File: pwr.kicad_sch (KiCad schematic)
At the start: 11 parts, among them U5 TPS561208DDCR

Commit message: Updated Schematic
Updated parts of todo list for schematic
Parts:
- added C5: .1uF, symbol Device:C_Small
- C1: value 44muF -> 22uF
- C2: value 20.1muF -> 22uF
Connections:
- net 12 V: now also C5.1
- net GND: now also C5.2
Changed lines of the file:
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@@
+	)
+	(junction
+		(at 62.23 41.91)
+		(diameter 0)
+		(color 0 0 0 0)
 	)
 	(junction
@@
 	(wire
 		(pts
-			(xy 49.53 41.91) (xy 66.04 41.91)
+			(xy 49.53 41.91) (xy 62.23 41.91)
 		)
 		(stroke
@@
 		(pts
 			(xy 157.48 26.67) (xy 157.48 46.99)
+		)
+		(stroke
+			(width 0)
+			(type default)
+		)
+	)
+	(wire
+		(pts
+			(xy 62.23 41.91) (xy 66.04 41.91)
 		)
 		(stroke
@@
 			)
 		)
-		(property "Value" "20.1muF"
+		(property "Value" "22uF"
 			(at 72.39 45.7262 0)
 			(show_name no)
@@
 			)
 		)
-		(property "Value" "44muF"
+		(property "Value" "22uF"
 			(at 137.16 40.6462 0)
 			(show_name no)
@@
 	)
 	(symbol
+		(lib_id "Device:C_Small")
+		(at 62.23 44.45 0)
+		(unit 1)
+		(body_style 1)
+		(exclude_from_sim no)
+		(in_bom yes)
+		(on_board yes)
+		(in_pos_files yes)
+		(dnp no)
+		(fields_autoplaced yes)
+		(property "Reference" "C5"
+			(at 64.77 43.1862 0)
+			(show_name no)
+			(do_not_autoplace no)
+			(effects
+				(font
+					(size 1.27 1.27)
+				)
+				(justify left)
+			)
+		)
+		(property "Value" ".1uF"
+			(at 64.77 45.7262 0)
+			(show_name no)
+			(do_not_autoplace no)
+			(effects
+				(font
+					(size 1.27 1.27)
+				)
+				(justify left)
+			)
+		)
+		(property "Footprint" ""
+			(at 62.23 44.45 0)
+			(hide yes)
+			(show_name no)
+			(do_not_autoplace no)
+			(effects
+				(font
+					(size 1.27 1.27)
+				)
+			)
+		)
+		(property "Datasheet" ""
+			(at 62.23 44.45 0)
+			(hide yes)
+			(show_name no)
+			(do_not_autoplace no)
+			(effects
+				(font
+					(size 1.27 1.27)
+				)
+			)
+		)
+		(property "Description" "Unpolarized capacitor, small symbol"
+			(at 62.23 44.45 0)
+			(hide yes)
+			(show_name no)
+			(do_not_autoplace no)
+			(effects
+				(font
+					(size 1.27 1.27)
+				)
+			)
+		)
+		(pin "2"
+		)
+		(pin "1"
+		)
+		(instances
+			(project "X19-Float-Board"
+				(path "/00000000-0000-0000-0000-000060e6118b/dfdc99bd-6797-4c58-8fa3-5fd2e2701b4c"
+					(reference "C5")
+					(unit 1)
+				)
+			)
+		)
+	)
+	(symbol
 		(lib_id "Device:R_Small_US")
 		(at 81.28 31.75 0)
@@
 					(unit 1)
 				)
+			)
+		)
+	)
+	(symbol
+		(lib_id "power:GND")
+		(at 62.23 46.99 0)
+		(unit 1)
+		(body_style 1)
+		(exclude_from_sim no)
+		(in_bom yes)
+		(on_board yes)
+		(in_pos_files yes)
+		(dnp no)
+		(fields_autoplaced yes)
+		(property "Reference" "#PWR029"
+			(at 62.23 53.34 0)
+			(hide yes)
+			(show_name no)
+			(do_not_autoplace no)
+			(effects
+				(font
+					(size 1.27 1.27)
+				)
+			)
+		)
+		(property "Value" "GND"
+			(at 62.23 52.07 0)
+			(show_name no)
+			(do_not_autoplace no)
+			(effects
+				(font
+					(size 1.27 1.27)
+				)
+			)
+		)
+		(property "Footprint" ""
+			(at 62.23 46.99 0)
+			(hide yes)
+			(show_name no)
+			(do_not_autoplace no)
+			(effects
+				(font
+					(size 1.27 1.27)
+				)
+			)
+		)
+		(property "Datasheet" ""
+			(at 62.23 46.99 0)
+			(hide yes)
+			(show_name no)
+			(do_not_autoplace no)
+			(effects
+				(font
+					(size 1.27 1.27)
+				)
+			)
+		)
+		(property "Description" "Power symbol creates a global label with name \"GND\" , ground"
+			(at 62.23 46.99 0)
+			(hide yes)
+			(show_name no)
+			(do_not_autoplace no)
+			(effects
+				(font
+					(size 1.27 1.27)
+				)
+			)
+		)
+		(pin "1"
+		)
+		(instances
+			(project "X19-Float-Board"
+				(path "/00000000-0000-0000-0000-000060e6118b/dfdc99bd-6797-4c58-8fa3-5fd2e2701b4c"
+					(reference "#PWR029")
+					(unit 1)
+				)

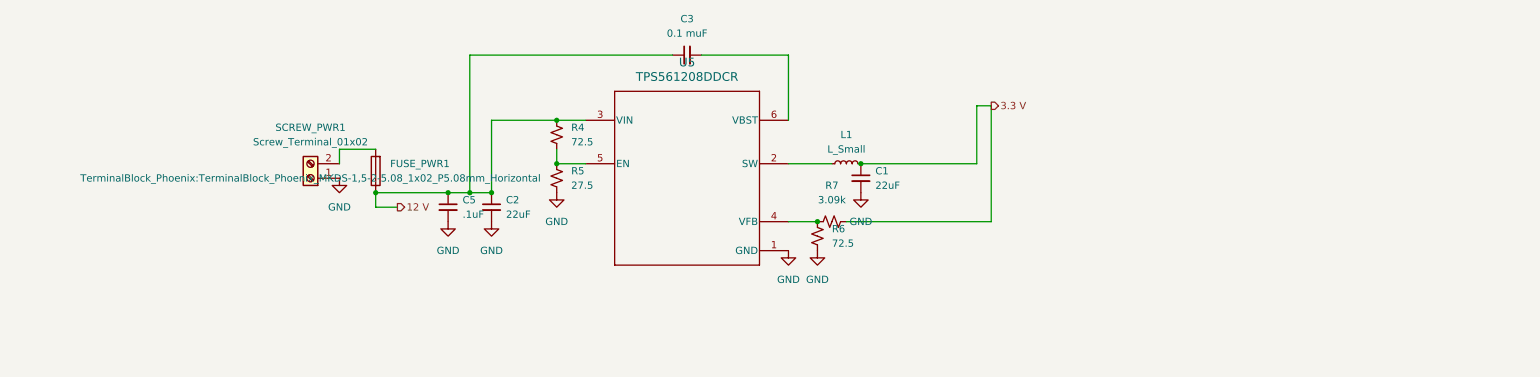
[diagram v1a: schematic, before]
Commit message: Updated Schematic
Updated schematic
Cleaned up dense portions
added H bridge
correct i2c wiring
added ferrite beads
added 12 V power monitoring
added stlink
added power mux
added power from usb
reformatted hierarichal sheets
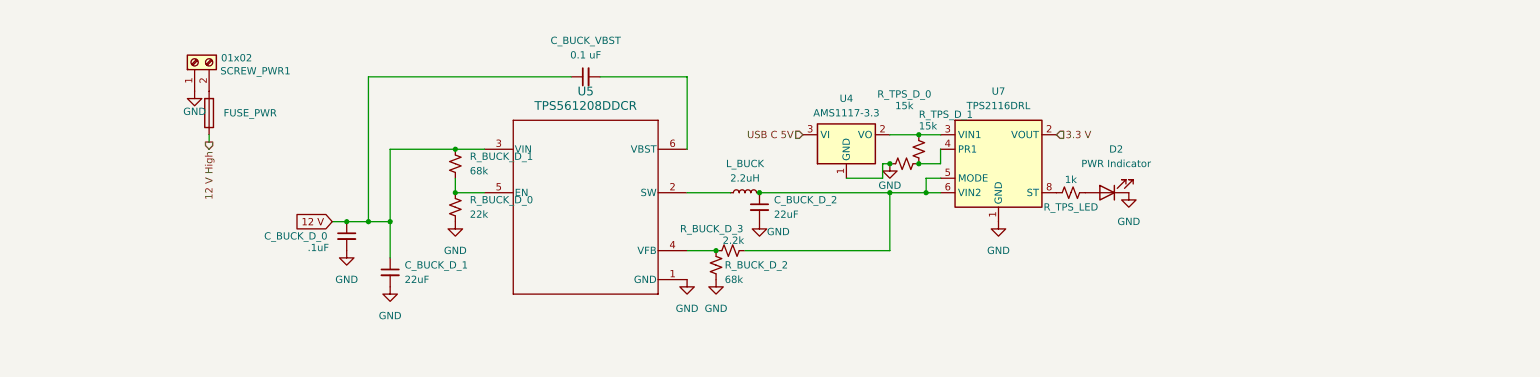
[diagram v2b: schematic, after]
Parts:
- added D2: PWR Indicator, symbol Device:LED
- added R_TPS_D_0, R_TPS_D_1: 15k, symbol Device:R_Small_US
- added R_TPS_LED: 1k, symbol Device:R_Small_US
- added U4: AMS1117-3.3, Package_TO_SOT_SMD:SOT-223-3_TabPin2, symbol Regulator_Linear:AMS1117-3.3
- added U7: TPS2116DRL, Package_TO_SOT_SMD:SOT-583-8, symbol Power_Management:TPS2116DRL
- C_BUCK_VBST: renamed from C3; value 0.1 muF -> 0.1 uF
- L_BUCK: renamed from L1; value L_Small -> 2.2uH
- R_BUCK_D_0: renamed from R5; value 27.5 -> 22k
- R_BUCK_D_1: renamed from R4; value 72.5 -> 68k
- R_BUCK_D_2: renamed from R6; value 72.5 -> 68k
- R_BUCK_D_3: renamed from R7; value 3.09k -> 2.2k
- SCREW_PWR1: value Screw_Terminal_01x02 -> 01x02
- renumbered C5 to C_BUCK_D_0, C2 to C_BUCK_D_1, C1 to C_BUCK_D_2, FUSE_PWR1 to FUSE_PWR
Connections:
- net 12 V: no longer FUSE_PWR.1
- net 3.3 V: now also U7.2 (VOUT), U7.7 (VOUT); no longer C_BUCK_D_2.1, L_BUCK.2, R_BUCK_D_3.2
- net GND: now also D2.1 (K), R_TPS_D_0.1, U4.1 (GND), U7.1 (GND)
- new net: R_TPS_D_1.1, U4.2 (VO), U7.3 (VIN1)
- new net: R_TPS_D_0.2, R_TPS_D_1.2, U7.4 (PR1)
- new net: C_BUCK_D_2.1, L_BUCK.2, R_BUCK_D_3.2, U7.5 (MODE), U7.6 (VIN2)
- new net: D2.2 (A), R_TPS_LED.2
- new net: R_TPS_LED.1, U7.8 (ST)
- new net 12 V High: FUSE_PWR.1
- new net USB C 5V: U4.3 (VI)
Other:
- moved on the sheet: C_BUCK_D_0, C_BUCK_D_1, C_BUCK_D_2, C_BUCK_VBST, FUSE_PWR, L_BUCK, R_BUCK_D_0, R_BUCK_D_1, R_BUCK_D_2, R_BUCK_D_3, SCREW_PWR1, U5

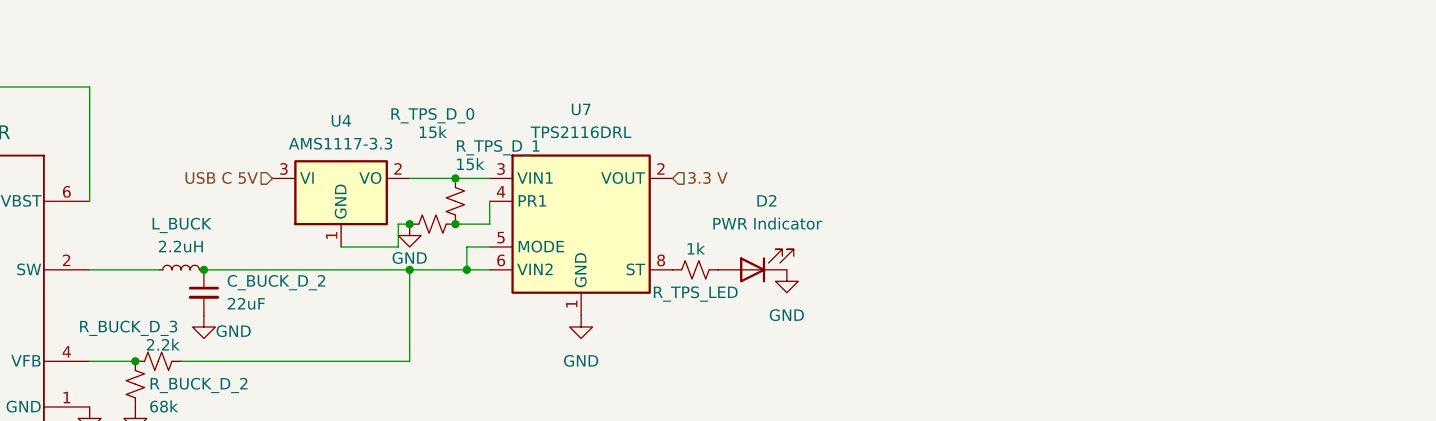
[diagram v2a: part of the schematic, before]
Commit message: USB, TVS, LDO, Passives, I2C
applied changes to usb circuitry, tvs, ldo, passibes and i2c.
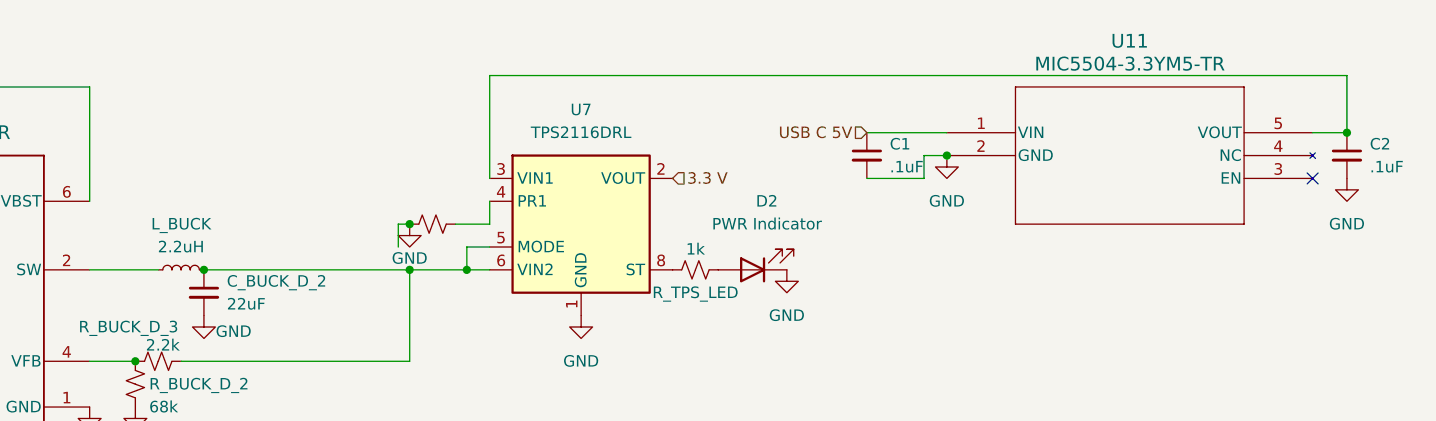
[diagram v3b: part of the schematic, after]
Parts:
- removed R_TPS_D_1: 15k, symbol Device:R_Small_US
- removed U4: AMS1117-3.3, Package_TO_SOT_SMD:SOT-223-3_TabPin2, symbol Regulator_Linear:AMS1117-3.3
- added C1, C2: .1uF, symbol Device:C_Small
- added U11: MIC5504-3.3YM5-TR, rov_power:SOT-23-5_MC_MCH, symbol rov_power:MIC5504-3.3YM5-TR
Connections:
- net GND: now also C1.2, C2.2, U11.2 (GND)
- net USB C 5V: now also C1.1, U11.1 (VIN)
- net at U7.3 (VIN1): now also C2.1, U11.5 (VOUT)
- no-connect marks 0 -> 1

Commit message: float
float for claude review
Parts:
- removed R_BUCK_D_0: 22k, symbol Device:R_Small_US
- removed R_BUCK_D_1: 68k, symbol Device:R_Small_US
- R_BUCK_D_2: value 68k -> 10k
- R_BUCK_D_3: value 2.2k -> 33.2k
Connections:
- net 12 V: now also U5.5 (EN)
- net USB C 5V: now also U11.3 (EN)
- no-connect marks 1 -> 0
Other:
- note added: "give enable 12 volts"

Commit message: footprints
footprints
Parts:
- removed C_BUCK_VBST: 0.1 uF, symbol Device:C_Small
- added C_BUCK_VBST1: 0.1 uF, Capacitor_SMD:C_0603_1608Metric_Pad1.08x0.95mm_HandSolder, symbol Device:C_Small
- C1, C2: value .1uF -> 1uF; footprint (none) -> Capacitor_SMD:C_0603_1608Metric_Pad1.08x0.95mm_HandSolder
- C_BUCK_D_0: footprint (none) -> Capacitor_SMD:C_0603_1608Metric_Pad1.08x0.95mm_HandSolder
- C_BUCK_D_1, C_BUCK_D_2: footprint (none) -> Capacitor_SMD:C_1210_3225Metric_Pad1.33x2.70mm_HandSolder
- D2: footprint (none) -> Capacitor_SMD:C_0805_2012Metric_Pad1.18x1.45mm_HandSolder
- L_BUCK1: renamed from L_BUCK; value 2.2uH -> 3.3uH
- U5: footprint DDC0006A_N -> CustomFootprints:DDC0006A_N
- renumbered FUSE_PWR to FUSE_PWR1, R_TPS_LED to R_TPS_LED1
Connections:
- net 3.3 V: now also D2.2 (A)
- net GND: no longer D2.1 (K)
- net at L_BUCK1.1, U5.2 (SW): now also C_BUCK_VBST1.2
- net at C_BUCK_D_2.1, L_BUCK1.2, R_BUCK_D_3.2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: now also U7.3 (VIN1); no longer U7.6 (VIN2)
- net at C2.1, U11.5 (VOUT): now also U7.6 (VIN2); no longer U7.3 (VIN1)
- net at R_TPS_LED1.2: now also D2.1 (K); no longer D2.2 (A)
- net at U5.6 (VBST): now also C_BUCK_VBST1.1
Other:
- note removed: "give enable 12 volts"

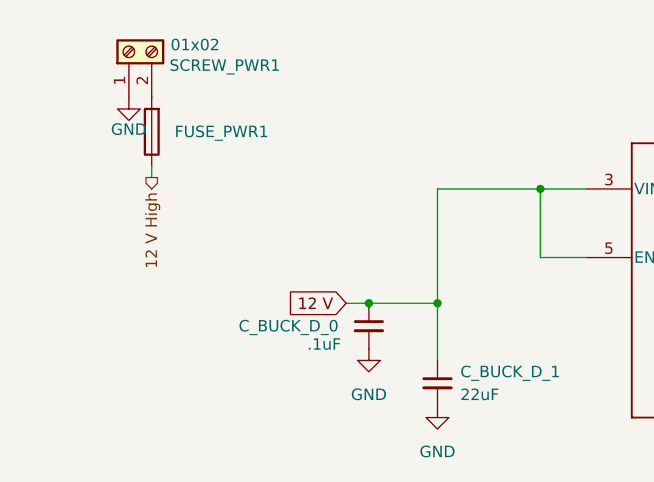
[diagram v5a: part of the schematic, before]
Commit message: Finished footprints
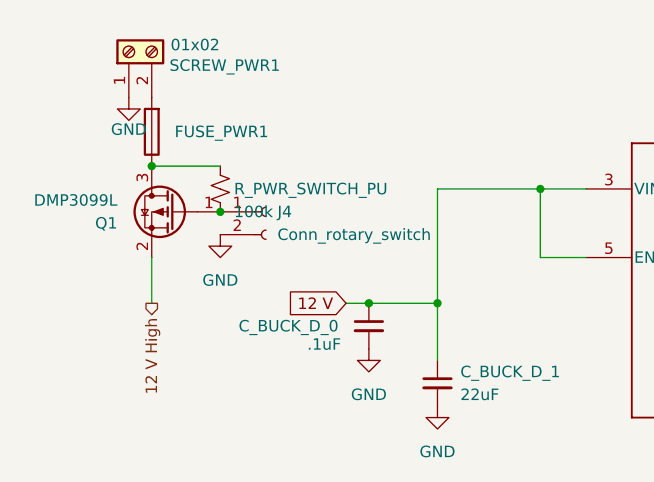
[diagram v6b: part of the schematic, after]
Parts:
- added J4: Conn_rotary_switch, symbol Connector:Conn_01x02_Socket
- added Q1: DMP3099L, Package_TO_SOT_SMD:SOT-23, symbol Transistor_FET:DMP3099L
- added R_PWR_SWITCH_PU: 100k, Resistor_SMD:R_0603_1608Metric_Pad0.98x0.95mm_HandSolder, symbol Device:R_Small_US
- L_BUCK1: footprint (none) -> Capacitor_SMD:C_0402_1005Metric_Pad0.74x0.62mm_HandSolder
- R_BUCK_D_2, R_BUCK_D_3, R_TPS_D_0, R_TPS_LED1: footprint (none) -> Resistor_SMD:R_0603_1608Metric_Pad0.98x0.95mm_HandSolder
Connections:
- net 12 V High: now also Q1.2 (S); no longer FUSE_PWR1.1
- net GND: now also J4.2 (Pin_2)
- new net: FUSE_PWR1.1, Q1.3 (D), R_PWR_SWITCH_PU.1
- new net: J4.1 (Pin_1), Q1.1 (G), R_PWR_SWITCH_PU.2
